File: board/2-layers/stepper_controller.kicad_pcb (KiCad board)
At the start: 2 copper layers, 34 parts, among them J201 USB_OTG, P103 M3_AOUT, P104 M3_BOUT, P105 M2_AOUT, P106 M2_BOUT, P107 M1_AOUT, P108 M1_BOUT, P201 UART1, P301 12V_Conn, U101 DRV8825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

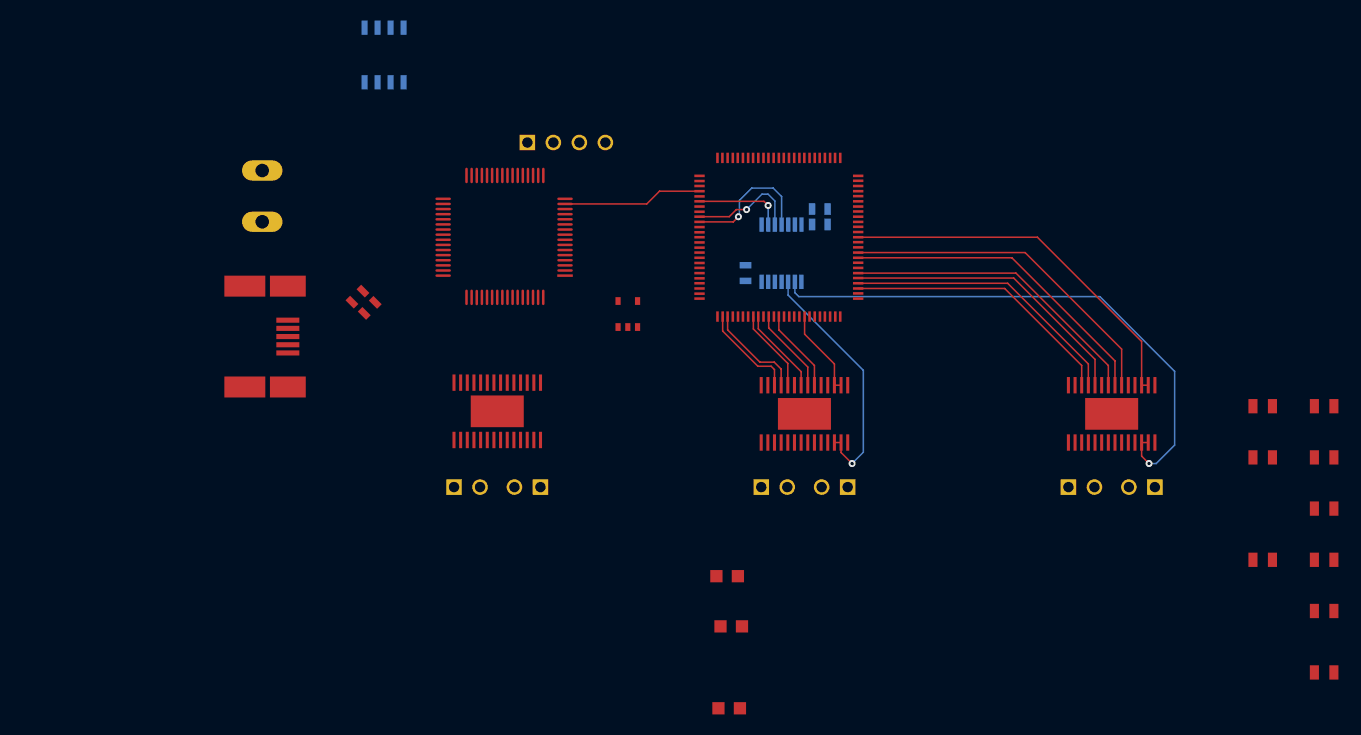
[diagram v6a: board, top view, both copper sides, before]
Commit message: Changed motor connector => 4 layers board
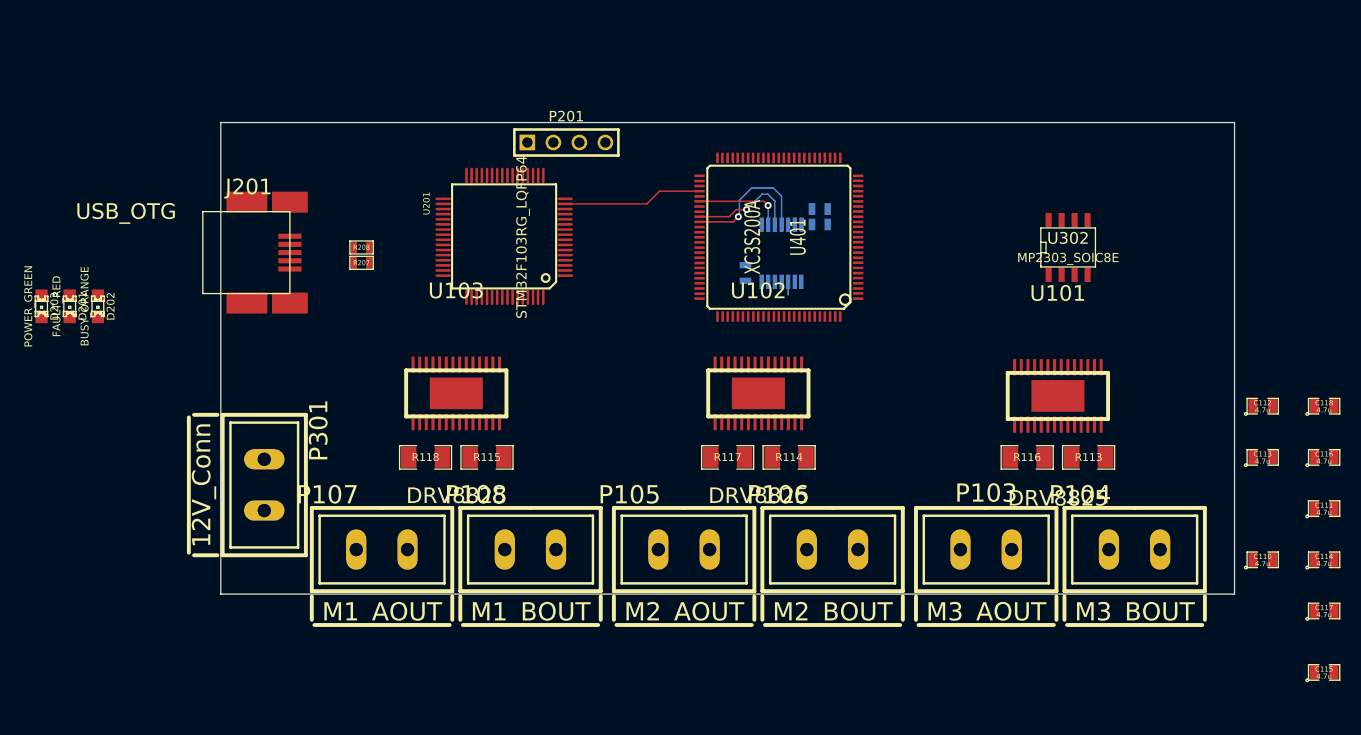
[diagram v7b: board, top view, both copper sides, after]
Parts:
- removed U301: MP2128-SOT23, SOT23-5
- added R113: 0.1, SM1206, F.Cu at (190.0, 119.0)
- added R114: 0.1, SM1206, F.Cu at (160.8, 119.0)
- added R115: 0.1, SM1206, F.Cu at (131.2, 119.0)
- added R116: 0.1, SM1206, F.Cu at (184.0, 119.0)
- added R117: 0.1, SM1206, F.Cu at (154.8, 119.0)
- added R118: 0.1, SM1206, F.Cu at (125.2, 119.0)
- P103, P104, P105, P106, P107, P108: footprint PIN_ARRAY_2X1 -> MOL_CONN_2_VH
- U302: moved to F.Cu
- moved D203 77.8 mm to (87.8, 104.2), turned to 270 degrees
- moved D201 69.4 mm to (90.5, 104.2), turned to 270 degrees
- moved U302 69.4 mm to (188.0, 98.5)
- moved D202 69.3 mm to (93.2, 104.2), turned to 270 degrees
- moved P301 28.2 mm to (109.5, 121.7)
- moved P103 11.1 mm to (180.0, 128.0)
- moved P105 10.7 mm to (150.5, 128.0)
- moved P107 10.3 mm to (121.0, 128.0)
- moved J201 8.20 mm to (108.0, 99.0)
- moved P104 6.14 mm to (194.5, 128.0), turned to 0 degrees
- moved P108 6.11 mm to (135.5, 128.0), turned to 0 degrees
- moved P106 6.10 mm to (165.0, 128.0), turned to 0 degrees
- moved U101 5.53 mm to (187.0, 113.0)
- moved U102 4.92 mm to (157.8, 112.8)
- moved R208 4.82 mm to (119.0, 98.5), turned to 0 degrees
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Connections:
- P104 pad 1: /MOT_B1_2 -> /MOT_B2_2
- P104 pad 2: /MOT_B2_2 -> /MOT_B1_2
- P106 pad 1: /MOT_B1_1 -> /MOT_B2_1
- P106 pad 2: /MOT_B2_1 -> /MOT_B1_1
- P108 pad 1: /MOT_B1_0 -> /MOT_B2_0
- P108 pad 2: /MOT_B2_0 -> /MOT_B1_0
- P301 pad 1: +12V -> GND
- P301 pad 2: GND -> +12V
- U401 pad 61: /FPGA/M0_EN -> /FPGA/M0_MODE2
- U401 pad 62: /FPGA/M0_RESET -> /FPGA/M0_MODE1
- U401 pad 64: /FPGA/M0_STEP -> /FPGA/M0_MODE0
- U401 pad 65: /FPGA/M0_DIR -> /FPGA/M0_STEP
- U401 pad 70: /FPGA/M0_MODE0 -> /FPGA/M0_EN
- U401 pad 71: /FPGA/M0_MODE1 -> /FPGA/M0_DIR
- U401 pad 72: /FPGA/M0_MODE2 -> /FPGA/M0_FAULT
- U401 pad 73: /FPGA/M0_FAULT -> /FPGA/M0_RESET
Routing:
- net /VRF_2: track 54.8 -> 0.00 mm, vias 1 -> 0
- net /FPGA/M2_RESET: track 36.8 -> 0.00 mm
- net /FPGA/M2_DIR: track 33.2 -> 0.00 mm
- net /FPGA/M2_EN: track 31.6 -> 0.00 mm
- net /FPGA/M2_STEP: track 30.1 -> 0.00 mm
- net /FPGA/M2_MODE0: track 28.9 -> 0.00 mm
- net /FPGA/M2_MODE1: track 27.8 -> 0.00 mm
- net /FPGA/M2_MODE2: track 26.9 -> 0.00 mm
- net /VRF_1: track 24.4 -> 1.30 mm, vias 1 -> 0
- net /FPGA/M1_MODE1: track 9.69 -> 0.00 mm
- net /FPGA/M1_MODE2: track 9.56 -> 0.00 mm
- net /FPGA/M1_RESET: track 8.56 -> 0.00 mm
- net /FPGA/M1_STEP: track 8.44 -> 0.00 mm
- net /FPGA/M1_EN: track 8.28 -> 0.00 mm
- net /FPGA/M1_DIR: track 8.14 -> 0.00 mm
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- added copper zone on GND, net GND
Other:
- board outline added: 99 x 46 mm
- copper layers 2 -> 4
- board text added: "PSU"

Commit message: boring commit message
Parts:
- added L302: 10uH, IND_7x7x4.5, F.Cu at (196.5, 96.5)
- added R101: NE, SM0603, F.Cu at (135.0, 111.0)
- added R102: NE, SM0603, F.Cu at (135.0, 114.5)
- added R103: NE, SM0603, F.Cu at (193.5, 111.0)
- added R104: NE, SM0603, F.Cu at (193.5, 115.0)
- added R105: NE, SM0603, F.Cu at (164.0, 114.5)
- added R106: NE, SM0603, F.Cu at (164.0, 111.0)
- added R203: ?, SM0603_Resistor, F.Cu at (111.5, 107.5)
- added R204: ?, SM0603_Resistor, F.Cu at (111.5, 110.0)
- added R205: ?, SM0603_Resistor, F.Cu at (111.5, 112.5)
- added R307: 10k, SM0603, F.Cu at (204.3, 132.4)
- added R308: 30.9k, SM0603, F.Cu at (204.3, 132.4)
- moved D203 21.9 mm to (108.0, 112.5), turned to 180 degrees
- moved D201 17.8 mm to (108.0, 107.5), turned to 180 degrees
- moved D202 15.8 mm to (108.0, 110.0), turned to 180 degrees
- moved U302 1.80 mm to (187.0, 97.0), turned to 90 degrees
- turned R208 to 180 degrees
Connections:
- D201 pad 1: N-0000093 (its old number) -> N-0000096
- D201 pad 2: N-0000092 (its old number) -> GND
- D202 pad 1: N-0000094 -> N-00000100
- D202 pad 2: N-0000098 -> GND
- D203 pad 1: N-0000095 -> N-0000098
- D203 pad 2: N-0000099 -> GND
- U201 pad 51: N-0000093 (its old number) -> N-00000101
- U201 pad 52: N-0000094 -> N-0000099
- U201 pad 53: N-0000095 -> N-0000097
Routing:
- net N-0000097: track 0.00 -> 23.6 mm
- net N-0000099: track 0.00 -> 22.0 mm
- net N-00000101: track 0.00 -> 20.5 mm
- net D-: track 0.00 -> 7.52 mm
- net D+: track 0.00 -> 7.31 mm
- net N-00000128: track 0.00 -> 6.65 mm
- net N-00000127: track 0.00 -> 6.36 mm
- net N-0000092: track 0.00 -> 6.08 mm
- net N-0000093: track 0.00 -> 3.62 mm
- net N-0000098: track 0.00 -> 1.69 mm
- net N-0000096: track 0.00 -> 1.69 mm
- net N-00000100: track 0.00 -> 1.69 mm
